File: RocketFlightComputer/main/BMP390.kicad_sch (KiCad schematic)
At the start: 3 parts

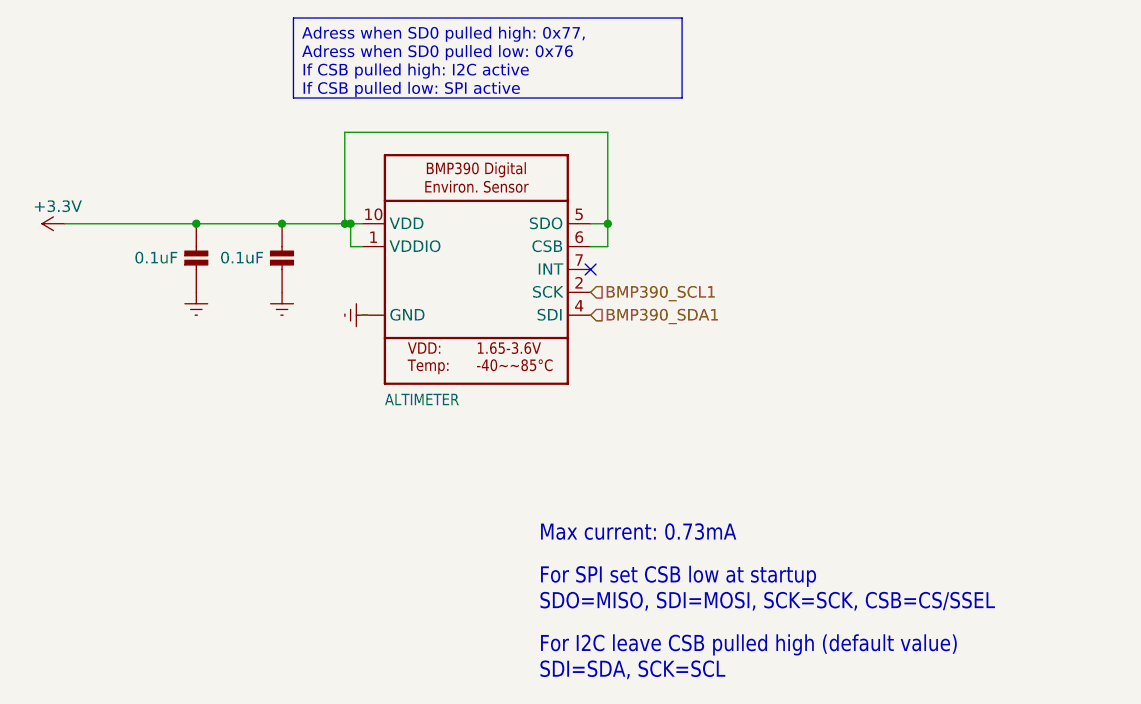
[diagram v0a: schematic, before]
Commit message: Corrections of mistake, revision of schematic is done and BOM revised, revision of pcb layout to do
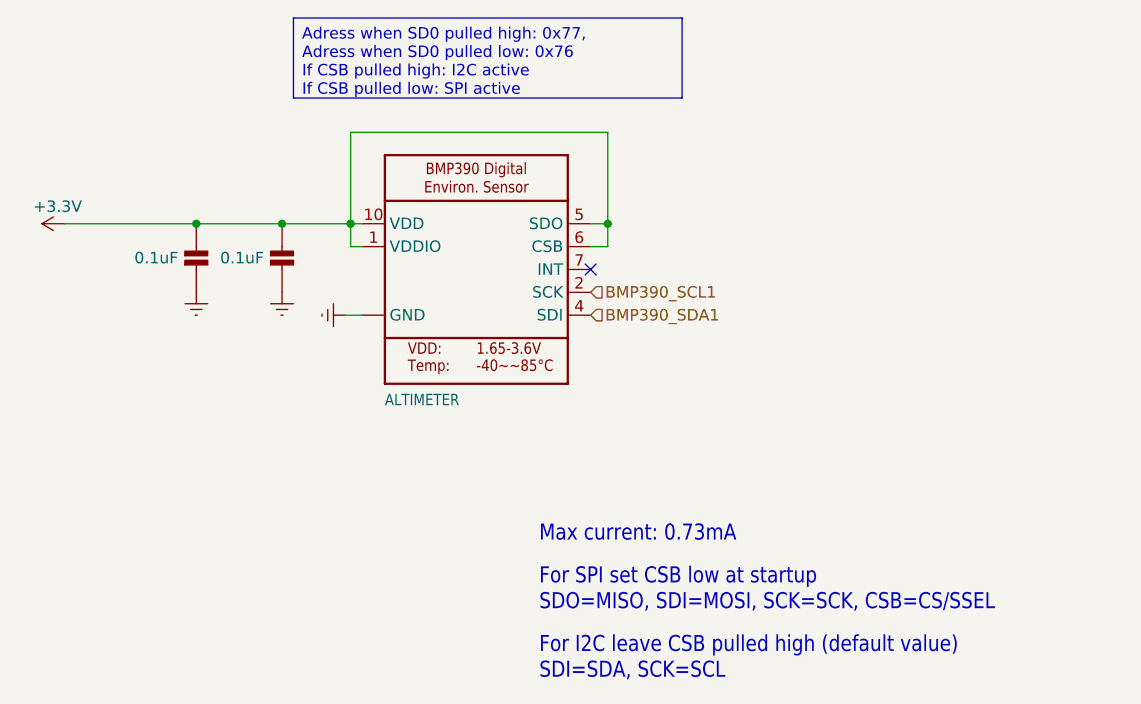
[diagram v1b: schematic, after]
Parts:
- C34, C35: LCSC C48579250 -> C1590
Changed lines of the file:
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@@
+	)
+	(junction
+		(at 88.265 53.34)
+		(diameter 0)
+		(color 0 0 0 0)
 	)
 	(junction
@@
 		(color 0 0 0 0)
 	)
-	(junction
-		(at 59.055 53.34)
-		(diameter 0)
-		(color 0 0 0 0)
-	)
-	(junction
-		(at 88.265 53.34)
-		(diameter 0)
-		(color 0 0 0 0)
-	)
 	(no_connect
 		(at 86.36 58.42)
@@
 	(wire
 		(pts
-			(xy 59.055 43.18) (xy 88.265 43.18)
+			(xy 88.265 53.34) (xy 86.36 53.34)
 		)
 		(stroke
@@
 	(wire
 		(pts
-			(xy 88.265 53.34) (xy 86.36 53.34)
+			(xy 59.69 53.34) (xy 60.96 53.34)
+		)
+		(stroke
+			(width 0.1524)
+			(type solid)
+		)
+	)
+	(wire
+		(pts
+			(xy 88.265 53.34) (xy 88.265 55.88)
 		)
 		(stroke
@@
 	(wire
 		(pts
-			(xy 59.69 53.34) (xy 59.055 53.34)
+			(xy 88.265 43.18) (xy 88.265 53.34)
+		)
+		(stroke
+			(width 0)
+			(type default)
+		)
+	)
+	(wire
+		(pts
+			(xy 52.07 53.34) (xy 59.69 53.34)
 		)
 		(stroke
@@
 	(wire
 		(pts
-			(xy 88.265 53.34) (xy 88.265 55.88)
+			(xy 27.94 53.34) (xy 42.545 53.34)
+		)
+		(stroke
+			(width 0.1524)
+			(type solid)
+		)
+	)
+	(wire
+		(pts
+			(xy 59.69 43.18) (xy 88.265 43.18)
 		)
 		(stroke
@@
 	(wire
 		(pts
-			(xy 88.265 43.18) (xy 88.265 53.34)
+			(xy 60.96 63.5) (xy 59.055 63.5)
 		)
 		(stroke
@@
 	(wire
 		(pts
-			(xy 52.07 53.34) (xy 59.055 53.34)
+			(xy 88.265 55.88) (xy 86.36 55.88)
+		)
+		(stroke
+			(width 0)
+			(type default)
+		)
+	)
+	(wire
+		(pts
+			(xy 42.545 53.34) (xy 52.07 53.34)
 		)
 		(stroke
@@
 	(wire
 		(pts
-			(xy 27.94 53.34) (xy 42.545 53.34)
+			(xy 60.96 55.88) (xy 59.69 55.88)
+		)
+		(stroke
+			(width 0)
+			(type default)
+		)
+	)
+	(wire
+		(pts
+			(xy 59.69 53.34) (xy 59.69 55.88)
 		)
 		(stroke
@@
 	(wire
 		(pts
-			(xy 60.96 63.5) (xy 61.595 63.5)
-		)
-		(stroke
-			(width 0)
-			(type default)
-		)
-	)
-	(wire
-		(pts
-			(xy 88.265 55.88) (xy 86.36 55.88)
-		)
-		(stroke
-			(width 0)
-			(type default)
-		)
-	)
-	(wire
-		(pts
-			(xy 42.545 53.34) (xy 52.07 53.34)
+			(xy 59.69 43.18) (xy 59.69 53.34)
 		)
 		(stroke
 			(width 0.1524)
 			(type solid)
-		)
-	)
-	(wire
-		(pts
-			(xy 60.96 55.88) (xy 59.69 55.88)
-		)
-		(stroke
-			(width 0)
-			(type default)
-		)
-	)
-	(wire
-		(pts
-			(xy 59.055 43.18) (xy 59.055 53.34)
-		)
-		(stroke
-			(width 0)
-			(type default)
-		)
-	)
-	(wire
-		(pts
-			(xy 60.96 53.34) (xy 59.69 53.34)
-		)
-		(stroke
-			(width 0.1524)
-			(type solid)
-		)
-	)
-	(wire
-		(pts
-			(xy 59.69 55.88) (xy 59.69 53.34)
-		)
-		(stroke
-			(width 0)
-			(type default)
 		)
 	)
@@
 			)
 		)
-		(property "LCSC" "C48579250"
+		(property "LCSC" "C1590"
 			(at 52.07 58.42 0)
 			(hide yes)
@@
 	(symbol
 		(lib_id "power:GNDREF")
-		(at 61.595 63.5 270)
+		(at 59.055 63.5 270)
 		(unit 1)
 		(body_style 1)
@@
 		(fields_autoplaced yes)
 		(property "Reference" "#PWR095"
-			(at 55.245 63.5 0)
+			(at 52.705 63.5 0)
 			(hide yes)
 			(show_name no)
@@
 		)
 		(property "Value" "GNDREF"
-			(at 57.785 62.865 90)
+			(at 55.245 62.865 90)
 			(hide yes)
 			(show_name no)
@@
 		)
 		(property "Footprint" ""
-			(at 61.595 63.5 0)
+			(at 59.055 63.5 0)
 			(hide yes)
 			(show_name no)
@@
 		)
 		(property "Datasheet" ""
-			(at 61.595 63.5 0)
+			(at 59.055 63.5 0)
 			(hide yes)
 			(show_name no)
@@
 		)
 		(property "Description" ""
-			(at 61.595 63.5 0)
+			(at 59.055 63.5 0)
 			(hide yes)
 			(show_name no)
@@
 			)
 		)
-		(property "LCSC" "C48579250"
+		(property "LCSC" "C1590"
 			(at 42.545 58.42 0)
 			(hide yes)
